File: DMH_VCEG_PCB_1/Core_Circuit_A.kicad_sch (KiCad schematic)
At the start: 104 parts, among them J21 Conn_01x10_PinHeader, J22 Conn_01x10_PinHeader, J24 Conn_01x06_PinHeader, Q1 BC558, Q10 BC548, Q2 BC558, Q3 BC548, Q4 BC548, Q5 MMBFJ113, Q6 MMBFJ113, Q7 BC548, Q8 BC548, Q9 BC548, SW1 SW_DPDT_x2_On-Off-(On), SW2 SW_DPDT_x2, SW3 SW_SPDT, U1 TL074, U2 4001, U22 CD4066BE, U3 40106, U4 CD4066BE, U5 TL074, U6 4001, U7 TL074

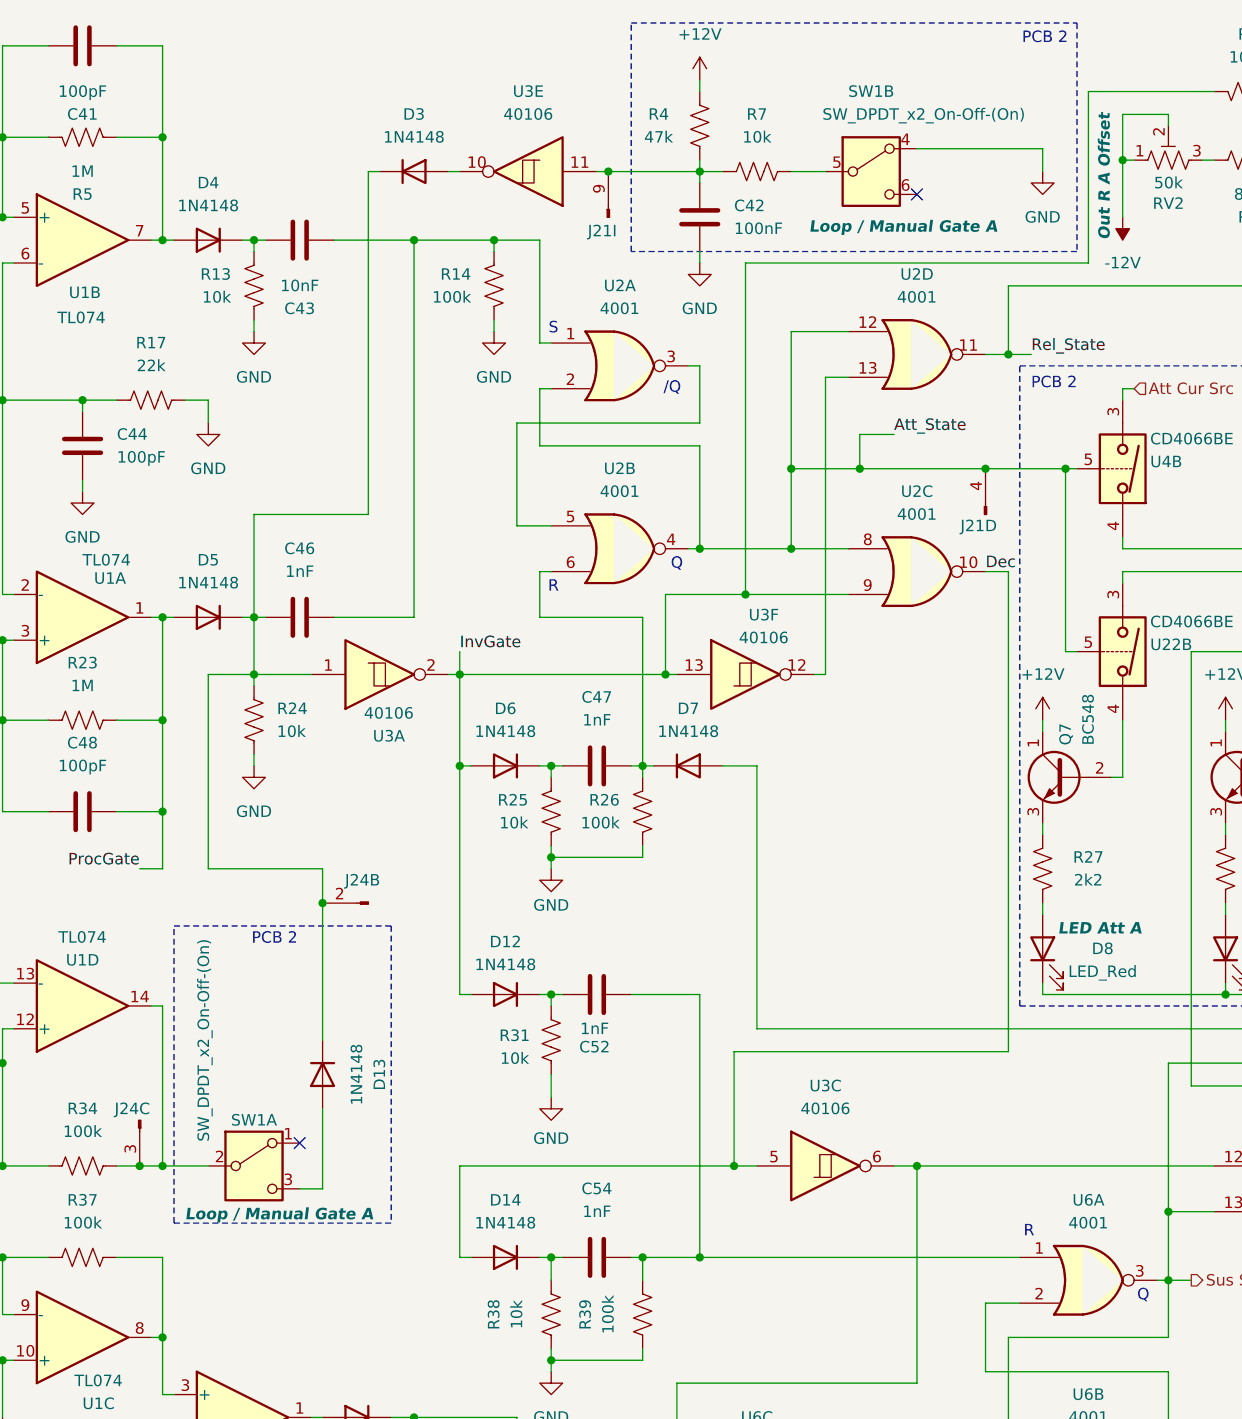
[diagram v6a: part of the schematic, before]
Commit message: Synced PCB 2 project with PCB 1
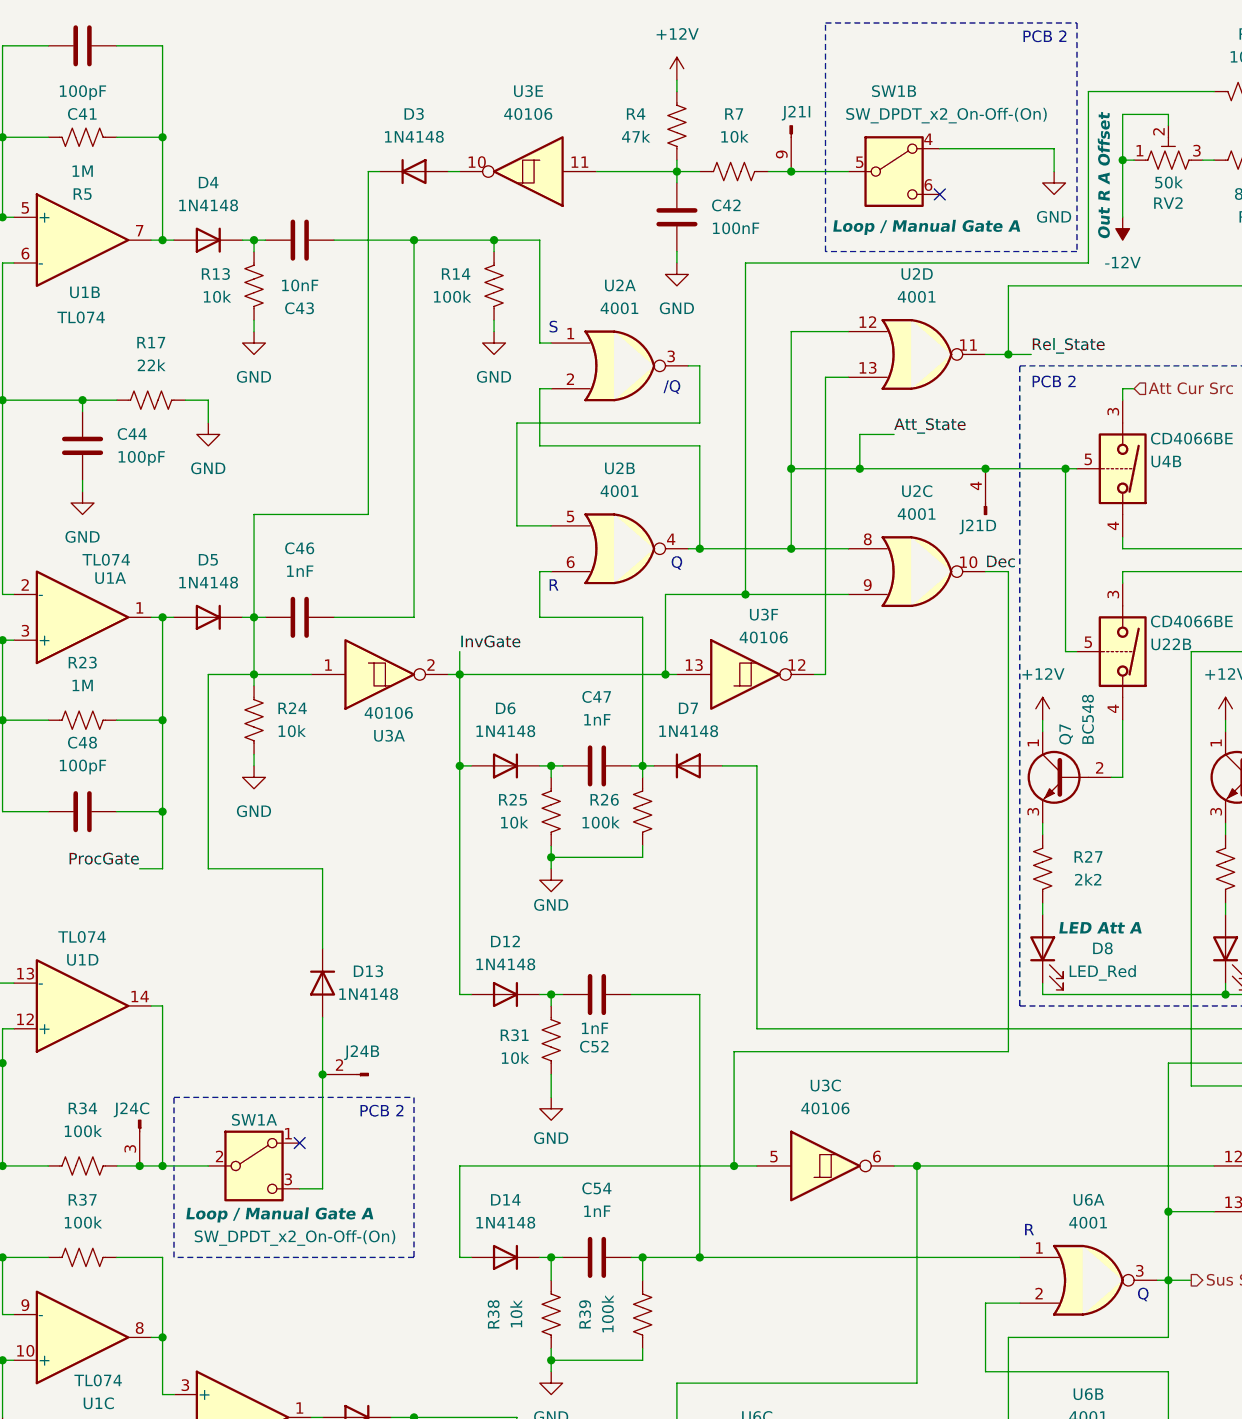
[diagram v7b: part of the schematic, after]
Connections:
- net at R7.1, SW1.5 (B): now also J21.9 (Pin_9)
- net at C42.1, R4.2, R7.2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: no longer J21.9 (Pin_9)
- net at C46.1, D13.1 (K), D3.1 (K)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: no longer J24.2 (Pin_2)
- net at D13.2 (A), SW1.3 (C): now also J24.2 (Pin_2)
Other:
- moved on the sheet: C42, D13, R4, R7, SW1B

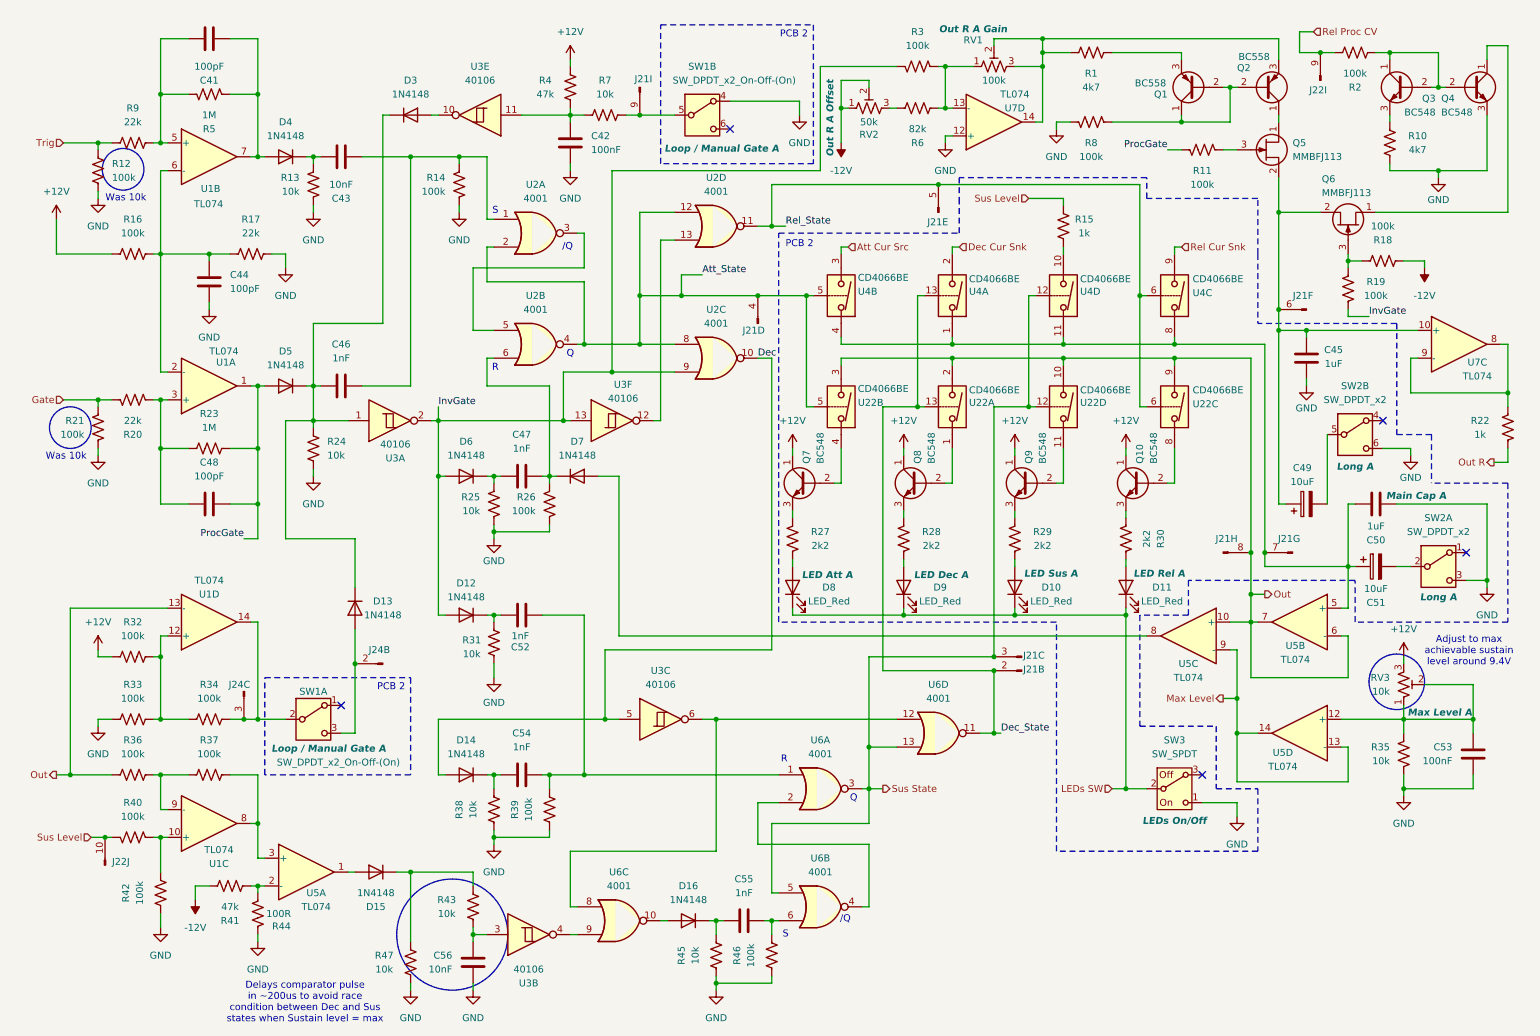
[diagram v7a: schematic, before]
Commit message: PCB 2 placement in progress
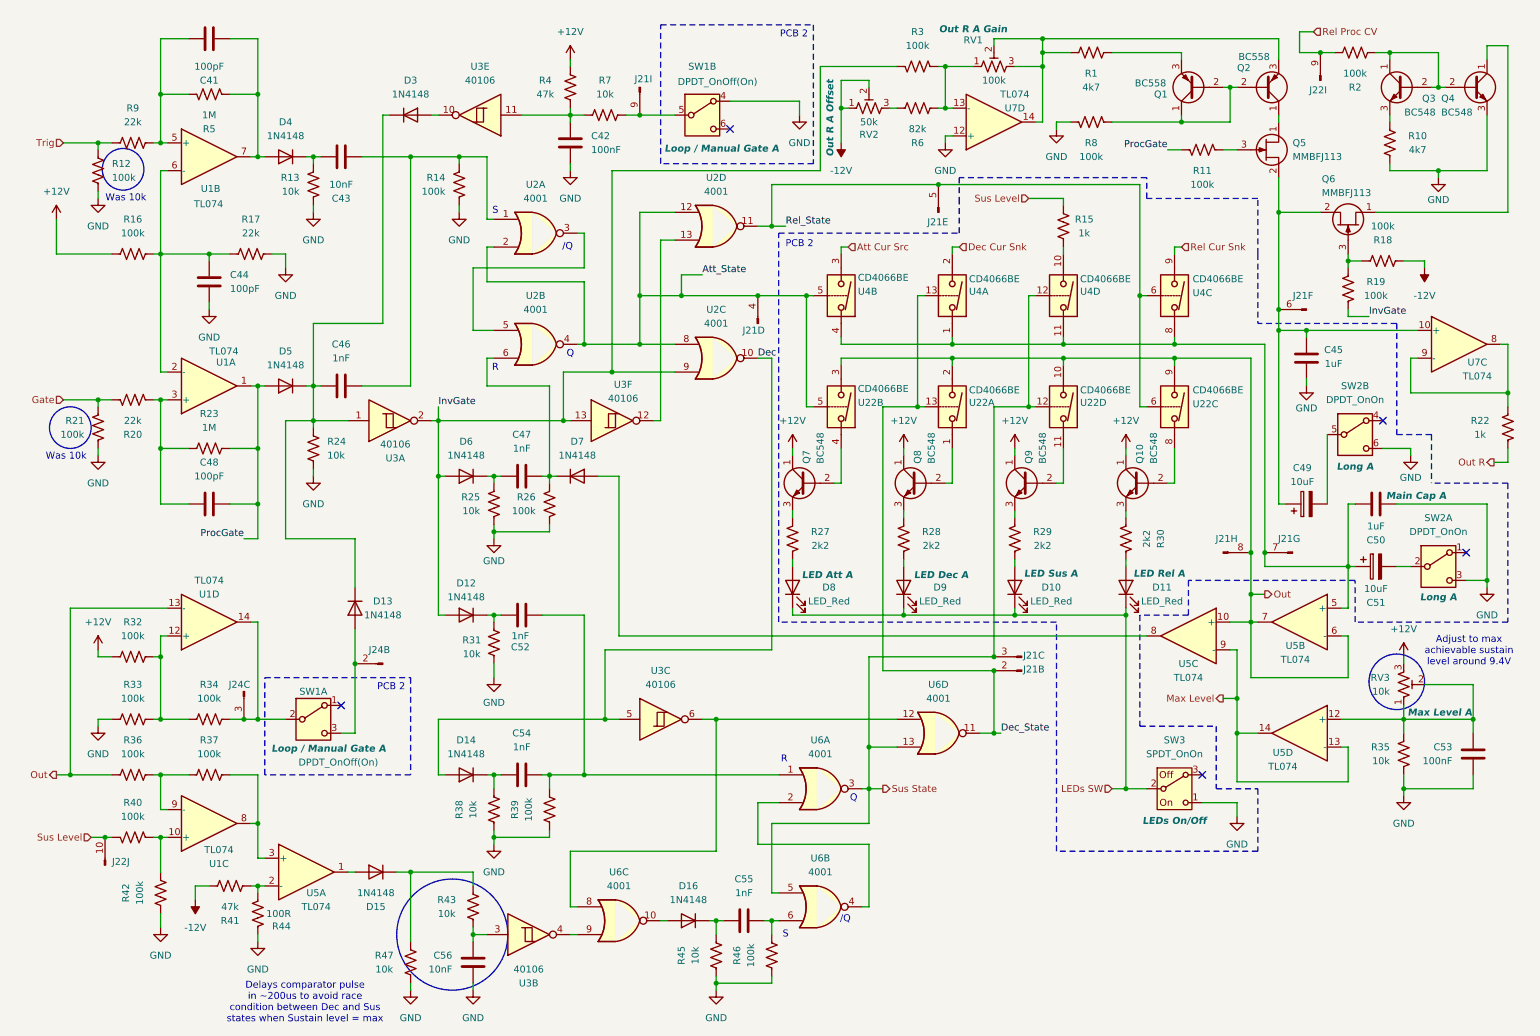
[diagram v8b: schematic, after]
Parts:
- SW1: value SW_DPDT_x2_On-Off-(On) -> DPDT_OnOff(On)
- SW2: value SW_DPDT_x2 -> DPDT_OnOn
- SW3: value SW_SPDT -> SPDT_OnOn
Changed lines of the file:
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@@
 			)
 		)
-		(property "Value" "SW_SPDT"
+		(property "Value" "SPDT_OnOn"
 			(at 222.25 147.32 0)
 			(effects
@@
 			)
 		)
-		(property "Value" "SW_DPDT_x2_On-Off-(On)"
-			(at 141.732 24.13 0)
+		(property "Value" "DPDT_OnOff(On)"
+			(at 138.684 24.384 0)
 			(effects
 				(font
@@
 			)
 		)
-		(property "Value" "SW_DPDT_x2"
+		(property "Value" "DPDT_OnOn"
 			(at 255.27 82.55 0)
 			(effects
@@
 			)
 		)
-		(property "Value" "SW_DPDT_x2_On-Off-(On)"
+		(property "Value" "DPDT_OnOff(On)"
 			(at 69.342 148.844 0)
 			(effects
@@
 			)
 		)
-		(property "Value" "SW_DPDT_x2"
+		(property "Value" "DPDT_OnOn"
 			(at 270.51 106.68 0)
 			(effects
